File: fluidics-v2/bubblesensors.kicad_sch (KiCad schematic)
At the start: 6 parts, among them U8 CD4050BDR, U9 TC7PZ17FU

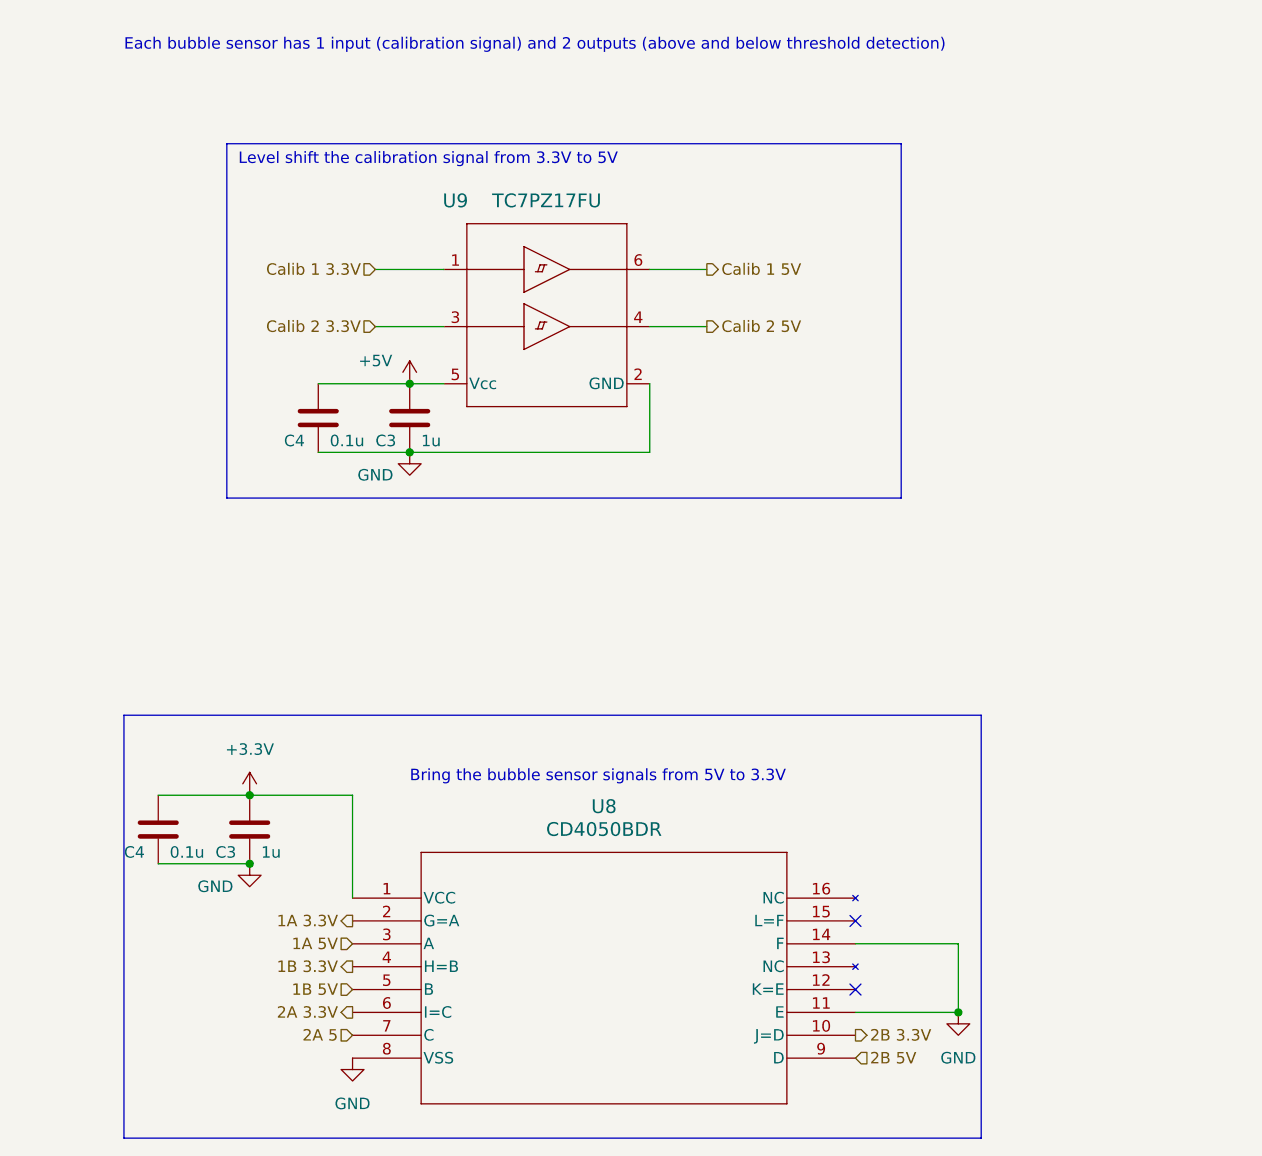
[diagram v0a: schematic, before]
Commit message: added footprints and mounting holes, cleaned up some sheets
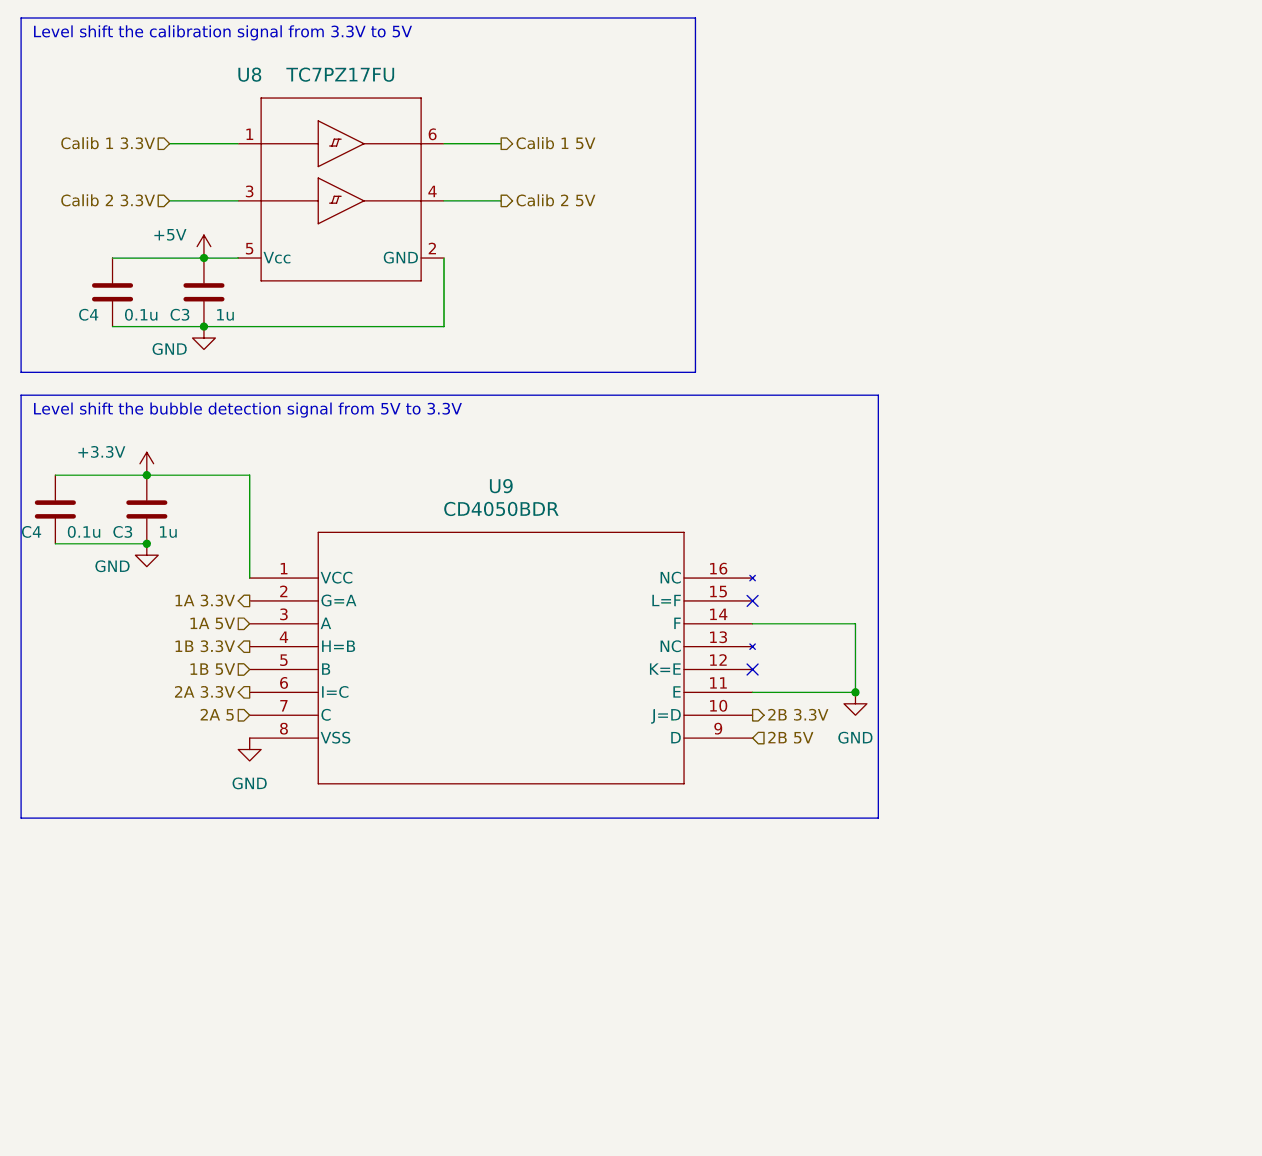
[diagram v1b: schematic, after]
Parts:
- renumbered U9 to U8, U8 to U9
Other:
- note added: "Level shift the bubble detection signal from 5V to 3.3V"
- note removed: "Bring the bubble sensor signals from 5V to 3.3V"
- note removed: "Each bubble sensor has 1 input (calibration signal) and 2 outputs (above and below threshold detection)"
- moved on the sheet: C3, C4, U8, U9
